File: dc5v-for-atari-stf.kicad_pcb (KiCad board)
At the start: 2 copper layers, 135 x 90 mm, 13 parts, among them J1 Conn_01x03, J2 Conn_01x06, J3 Adjustable MT3608 module, J4 Fixed 12V module, J5 Conn_01x02, SW1 Momentary or Latched

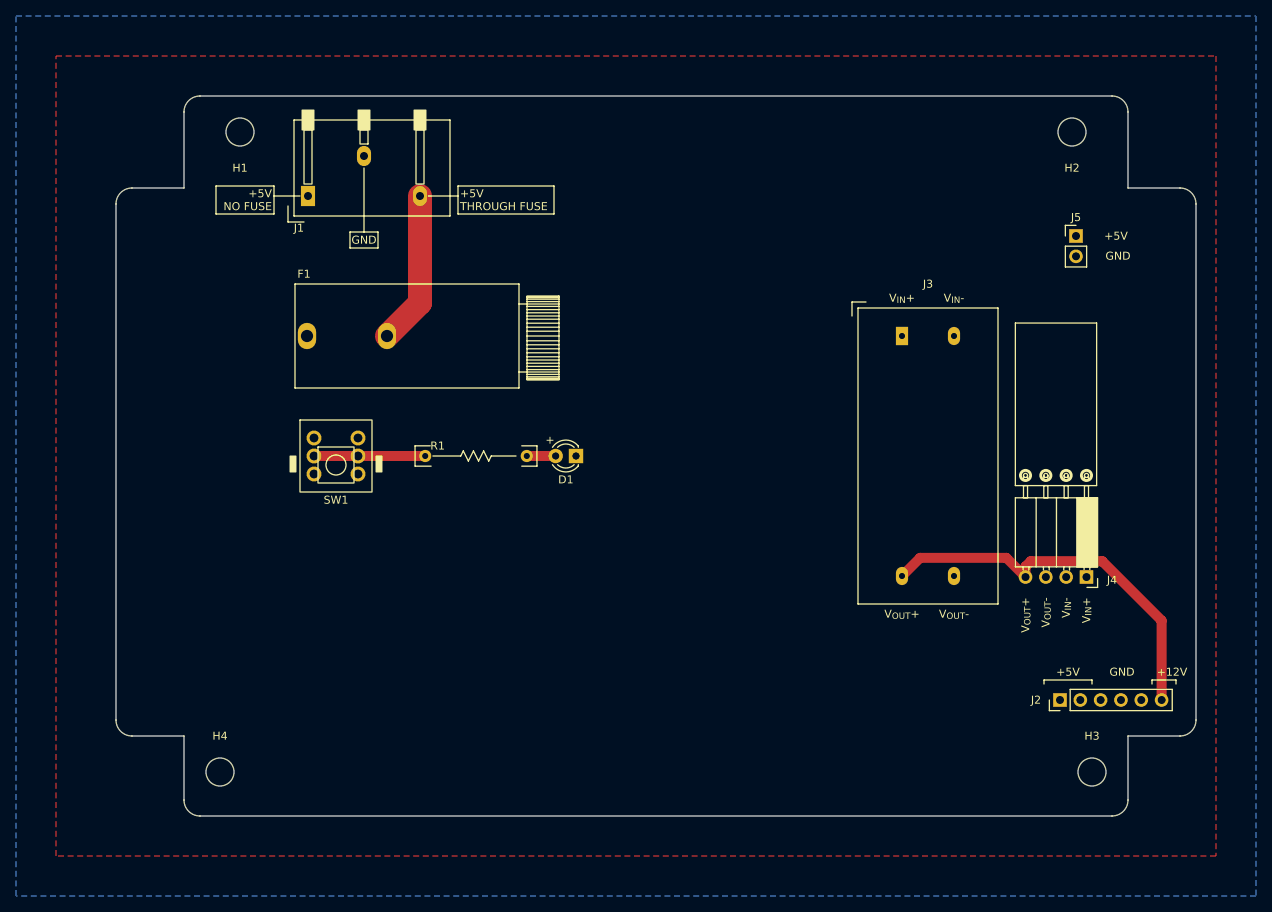
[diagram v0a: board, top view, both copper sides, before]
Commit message: Additionnal markings, tweaks on labels,...
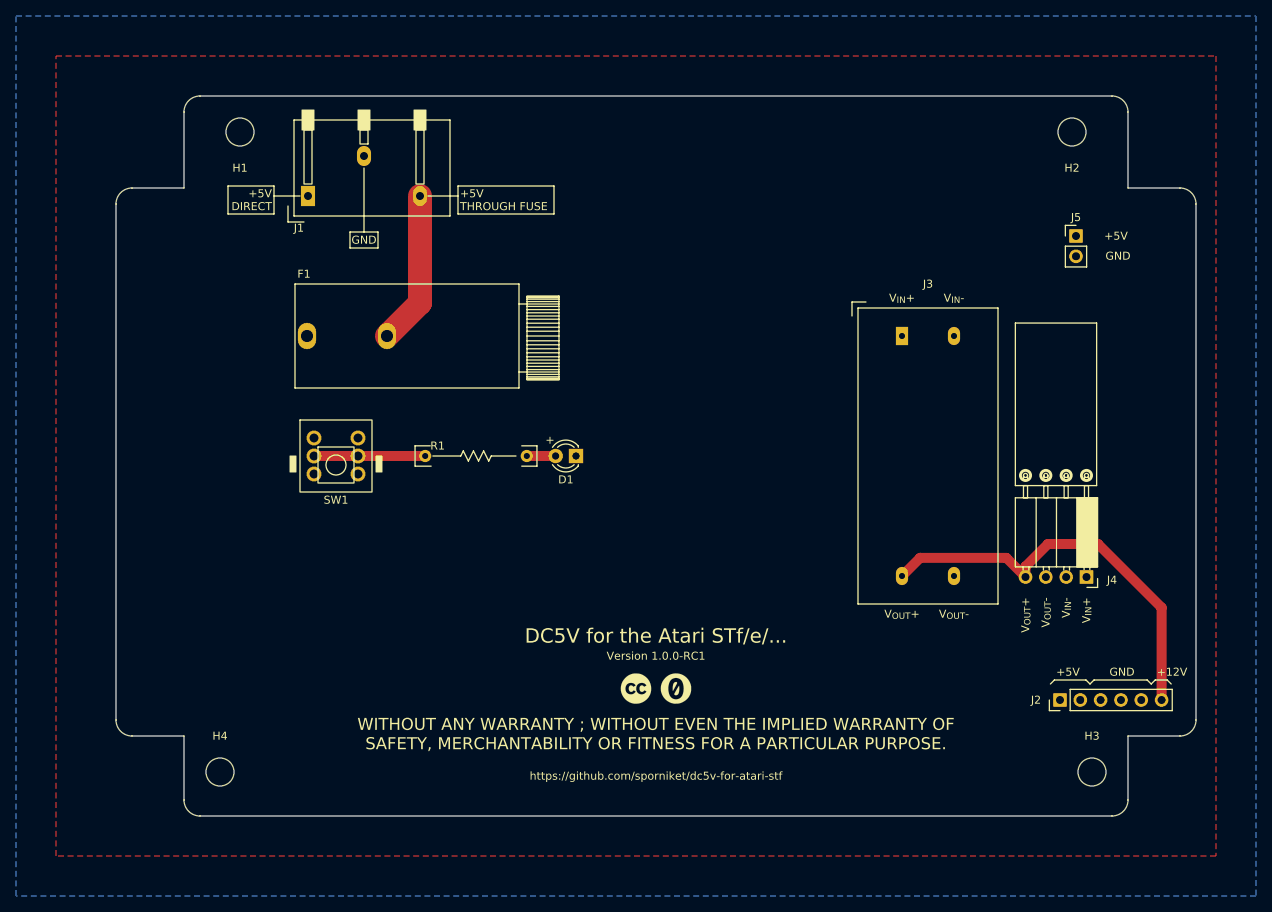
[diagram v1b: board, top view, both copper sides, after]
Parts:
- added G***: LOGO, cliparts:logo--cc--cc, F.Cu at (147.5, 129.1)
- added G***: LOGO, cliparts:logo--cc--zero, F.Cu at (152.5, 129.1)
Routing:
- net +12V: track 49.0 -> 51.7 mm
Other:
- board text added: "+5V DIRECT"
- board text added: "DC5V for the Atari STf/e/..."
- board text added: "Version 1.0.0-RC1"
- board text added: "WITHOUT ANY WARRANTY ; WITHOUT EVEN THE IMPLIED WARRANTY OF SAFETY, MERCHANTABILITY OR FITNESS FOR A PARTICULAR PURPOSE."
- board text added: "https://github.com/sporniket/dc5v-for-atari-stf"
- board text removed: "+5V NO FUSE"

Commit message: bump version
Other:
- board text added: "Version 1.0.0-RC2"
- board text removed: "Version 1.0.0-RC1"
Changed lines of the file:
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@@
     (title "DC5V for the Atari STf/e/...")
     (date "2023-08-24")
-    (rev "v1.0.0-RC1")
+    (rev "v1.0.0-RC2")
     (company "Sporniket")
     (comment 4 "https://github.com/sporniket/dc5v-for-atari-stf")
@@
   (gr_arc (start 91 57) (mid 91.585786 55.585786) (end 93 55) (layer "Edge.Cuts") (width 0.1))
   (gr_line (start 93 145) (end 207 145) (layer "Edge.Cuts") (width 0.1))
-  (gr_text "Version 1.0.0-RC1" (at 150 125) (layer "F.SilkS")
+  (gr_text "Version 1.0.0-RC2" (at 150 125) (layer "F.SilkS")
     (effects (font (size 1 1) (thickness 0.15)))
   )

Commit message: additionnal marking
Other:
- board text added: "POWER ON"
- board text added: "Test DC 5V wiring Show Power ON"
- board text added: "USE NYLON SCREW WASHER AT EACH MOUNTING HOLE !"
- board text added: "USE ONLY ONE 5V→12V MODULE !"
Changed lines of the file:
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@@
     (property "Sheetname" "")
     (attr through_hole)
-    (fp_text reference "J3" (at 0 -21.5 unlocked) (layer "F.SilkS")
+    (fp_text reference "J3" (at -8.6 -20.5 unlocked) (layer "F.SilkS")
       (effects (font (size 1 1) (thickness 0.15)))
     )
@@
   (gr_line (start 96.5 66.25) (end 96.5 69.75) (layer "F.SilkS") (width 0.15))
   (gr_line (start 211.9 128.5) (end 211.4 128) (layer "F.SilkS") (width 0.15))
+  (gr_line (start 172 72) (end 172 80) (layer "F.SilkS") (width 0.15))
+  (gr_line (start 172 76) (end 182 76) (layer "F.SilkS") (width 0.15))
   (gr_line (start 102.25 66.25) (end 96.5 66.25) (layer "F.SilkS") (width 0.15))
   (gr_line (start 199.8 128) (end 203.75 128) (layer "F.SilkS") (width 0.15))
   (gr_line (start 102.25 69.75) (end 102.25 66.25) (layer "F.SilkS") (width 0.15))
   (gr_line (start 125.25 67.5) (end 121.5 67.5) (layer "F.SilkS") (width 0.15))
+  (gr_line (start 184 78) (end 184 81.5) (layer "F.SilkS") (width 0.15))
+  (gr_line (start 196.8 76) (end 200 79.2) (layer "F.SilkS") (width 0.15))
   (gr_line (start 105.5 67.5) (end 102.25 67.5) (layer "F.SilkS") (width 0.15))
   (gr_line (start 125.25 66.25) (end 137.25 66.25) (layer "F.SilkS") (width 0.15))
@@
   (gr_line (start 113.5 64) (end 113.5 72) (layer "F.SilkS") (width 0.15))
   (gr_line (start 204.25 128.5) (end 204.75 128) (layer "F.SilkS") (width 0.15))
+  (gr_line (start 172 80) (end 154.2 80) (layer "F.SilkS") (width 0.15))
   (gr_line (start 111.75 72) (end 115.25 72) (layer "F.SilkS") (width 0.15))
   (gr_line (start 203.75 128) (end 204.25 128.5) (layer "F.SilkS") (width 0.15))
+  (gr_line (start 108 110.2) (end 108 104.4) (layer "F.SilkS") (width 0.15))
   (gr_line (start 111.75 74) (end 111.75 72) (layer "F.SilkS") (width 0.15))
   (gr_line (start 204.75 128) (end 211.4 128) (layer "F.SilkS") (width 0.15))
@@
   (gr_line (start 125.25 69.75) (end 125.25 66.25) (layer "F.SilkS") (width 0.15))
   (gr_line (start 115.25 72) (end 115.25 74) (layer "F.SilkS") (width 0.15))
+  (gr_line (start 182 76) (end 184 78) (layer "F.SilkS") (width 0.15))
+  (gr_rect (start 100.8 114) (end 115.2 110.2) (layer "F.SilkS") (width 0.15) (fill none))
   (gr_line (start 214.4 128.5) (end 213.9 128) (layer "F.SilkS") (width 0.15))
   (gr_line (start 137.25 66.25) (end 137.25 69.75) (layer "F.SilkS") (width 0.15))
+  (gr_line (start 154.2 80) (end 154.2 72) (layer "F.SilkS") (width 0.15))
+  (gr_line (start 182 76) (end 196.8 76) (layer "F.SilkS") (width 0.15))
   (gr_line (start 211.9 128.5) (end 212.4 128) (layer "F.SilkS") (width 0.15))
   (gr_line (start 115.25 74) (end 111.75 74) (layer "F.SilkS") (width 0.15))
+  (gr_line (start 200 79.2) (end 200 83.38) (layer "F.SilkS") (width 0.15))
+  (gr_line (start 154.2 72) (end 172 72) (layer "F.SilkS") (width 0.15))
   (gr_line (start 213.9 128) (end 212.4 128) (layer "F.SilkS") (width 0.15))
   (gr_line (start 137.25 69.75) (end 125.25 69.75) (layer "F.SilkS") (width 0.15))
@@
     (effects (font (size 1 1) (thickness 0.15)))
   )
+  (gr_text "USE ONLY ONE\n5V→12V \nMODULE !" (at 163 76) (layer "F.SilkS")
+    (effects (font (size 1.5 1.5) (thickness 0.25)))
+  )
   (gr_text "+5V" (at 201.5 127) (layer "F.SilkS")
     (effects (font (size 1 1) (thickness 0.15)))
@@
     (effects (font (size 1 1) (thickness 0.15)))
   )
+  (gr_text "POWER ON" (at 138.6 104.6) (layer "F.SilkS")
+    (effects (font (size 1 1) (thickness 0.15)))
+  )
   (gr_text "GND" (at 113.5 73) (layer "F.SilkS")
     (effects (font (size 1 1) (thickness 0.15)))
   )
+  (gr_text "USE NYLON SCREW WASHER AT EACH MOUNTING HOLE !" (at 162.8 60) (layer "F.SilkS")
+    (effects (font (size 1.25 1.25) (thickness 0.225)))
+  )
   (gr_text "+12V" (at 214.5 127) (layer "F.SilkS")
+    (effects (font (size 1 1) (thickness 0.15)))
+  )
+  (gr_text "Test DC 5V wiring\nShow Power ON" (at 108 112) (layer "F.SilkS")
     (effects (font (size 1 1) (thickness 0.15)))
   )
@@
     )
   )
+  (group "" (id 470b6958-64d2-4b93-bc38-bfed23ddec68)
+    (members
+      1804e07a-985b-4158-b38e-f605143f2194
+      36786f1c-5181-4b16-85f0-7a9b5e48989f
+      762c3c0b-490f-4700-be51-c6a7ba896fe3
+      ca1af6e0-b911-4719-a936-e41d586110b5
+      e3898bcd-ba25-495d-bce5-2258be9d151b
+    )
+  )
   (group "" (id 5a5a7337-565c-494f-973c-49547247a8e4)
     (members
@@
     )
   )
+  (group "" (id 5f6fbc87-cd39-4d24-8f5c-dad4bc9df885)
+    (members
+      ab866081-8f8b-49e6-ab59-50933150a879
+      ce5389af-7ae4-4674-b884-f51de059ed49
+    )
+  )

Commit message: prepare next release
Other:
- board text added: "USE NYLON SCREW WASHERS AT EACH MOUNTING HOLE !"
- board text removed: "USE NYLON SCREW WASHER AT EACH MOUNTING HOLE !"
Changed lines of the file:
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@@
   (title_block
     (title "DC5V for the Atari STf/e/...")
-    (date "2023-08-24")
+    (date "2023-08-26")
     (rev "v1.0.0-RC2")
     (company "Sporniket")
@@
   (gr_line (start 172 76) (end 182 76) (layer "F.SilkS") (width 0.15))
   (gr_line (start 102.25 66.25) (end 96.5 66.25) (layer "F.SilkS") (width 0.15))
+  (gr_rect (start 166 57.2) (end 194 61.6) (layer "F.SilkS") (width 0.15) (fill none))
   (gr_line (start 199.8 128) (end 203.75 128) (layer "F.SilkS") (width 0.15))
   (gr_line (start 102.25 69.75) (end 102.25 66.25) (layer "F.SilkS") (width 0.15))
   (gr_line (start 125.25 67.5) (end 121.5 67.5) (layer "F.SilkS") (width 0.15))
+  (gr_line (start 205.7 72.5) (end 203.4 72.5) (layer "F.SilkS") (width 0.15))
   (gr_line (start 184 78) (end 184 81.5) (layer "F.SilkS") (width 0.15))
   (gr_line (start 196.8 76) (end 200 79.2) (layer "F.SilkS") (width 0.15))
@@
   (gr_line (start 113.5 64) (end 113.5 72) (layer "F.SilkS") (width 0.15))
   (gr_line (start 204.25 128.5) (end 204.75 128) (layer "F.SilkS") (width 0.15))
+  (gr_line (start 209.4 73.4) (end 206.6 73.4) (layer "F.SilkS") (width 0.15))
   (gr_line (start 172 80) (end 154.2 80) (layer "F.SilkS") (width 0.15))
   (gr_line (start 111.75 72) (end 115.25 72) (layer "F.SilkS") (width 0.15))
+  (gr_line (start 209.4 71.6) (end 209.4 73.4) (layer "F.SilkS") (width 0.15))
   (gr_line (start 203.75 128) (end 204.25 128.5) (layer "F.SilkS") (width 0.15))
   (gr_line (start 108 110.2) (end 108 104.4) (layer "F.SilkS") (width 0.15))
   (gr_line (start 111.75 74) (end 111.75 72) (layer "F.SilkS") (width 0.15))
   (gr_line (start 204.75 128) (end 211.4 128) (layer "F.SilkS") (width 0.15))
+  (gr_line (start 194 59.4) (end 200.4 59.4) (layer "F.SilkS") (width 0.15))
+  (gr_line (start 206.6 73.4) (end 205.7 72.5) (layer "F.SilkS") (width 0.15))
   (gr_line (start 199.3 128.5) (end 199.8 128) (layer "F.SilkS") (width 0.15))
   (gr_line (start 125.25 69.75) (end 125.25 66.25) (layer "F.SilkS") (width 0.15))
@@
   (gr_line (start 211.9 128.5) (end 212.4 128) (layer "F.SilkS") (width 0.15))
   (gr_line (start 115.25 74) (end 111.75 74) (layer "F.SilkS") (width 0.15))
+  (gr_line (start 206.6 71.6) (end 209.4 71.6) (layer "F.SilkS") (width 0.15))
+  (gr_line (start 205.7 72.5) (end 206.6 71.6) (layer "F.SilkS") (width 0.15))
   (gr_line (start 200 79.2) (end 200 83.38) (layer "F.SilkS") (width 0.15))
   (gr_line (start 154.2 72) (end 172 72) (layer "F.SilkS") (width 0.15))
@@
     (effects (font (size 1 1) (thickness 0.15)))
   )
-  (gr_text "USE NYLON SCREW WASHER AT EACH MOUNTING HOLE !" (at 162.8 60) (layer "F.SilkS")
+  (gr_text "USE NYLON SCREW WASHERS\nAT EACH MOUNTING HOLE !" (at 180 59.4) (layer "F.SilkS")
     (effects (font (size 1.25 1.25) (thickness 0.225)))
   )
